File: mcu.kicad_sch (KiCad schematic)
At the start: 14 parts, among them J2 DevKit J1, J3 DevKit J3, J4 I2C / Qwiic, J5 WS2812, J6 Rail break-out, U2 74AHCT1G125

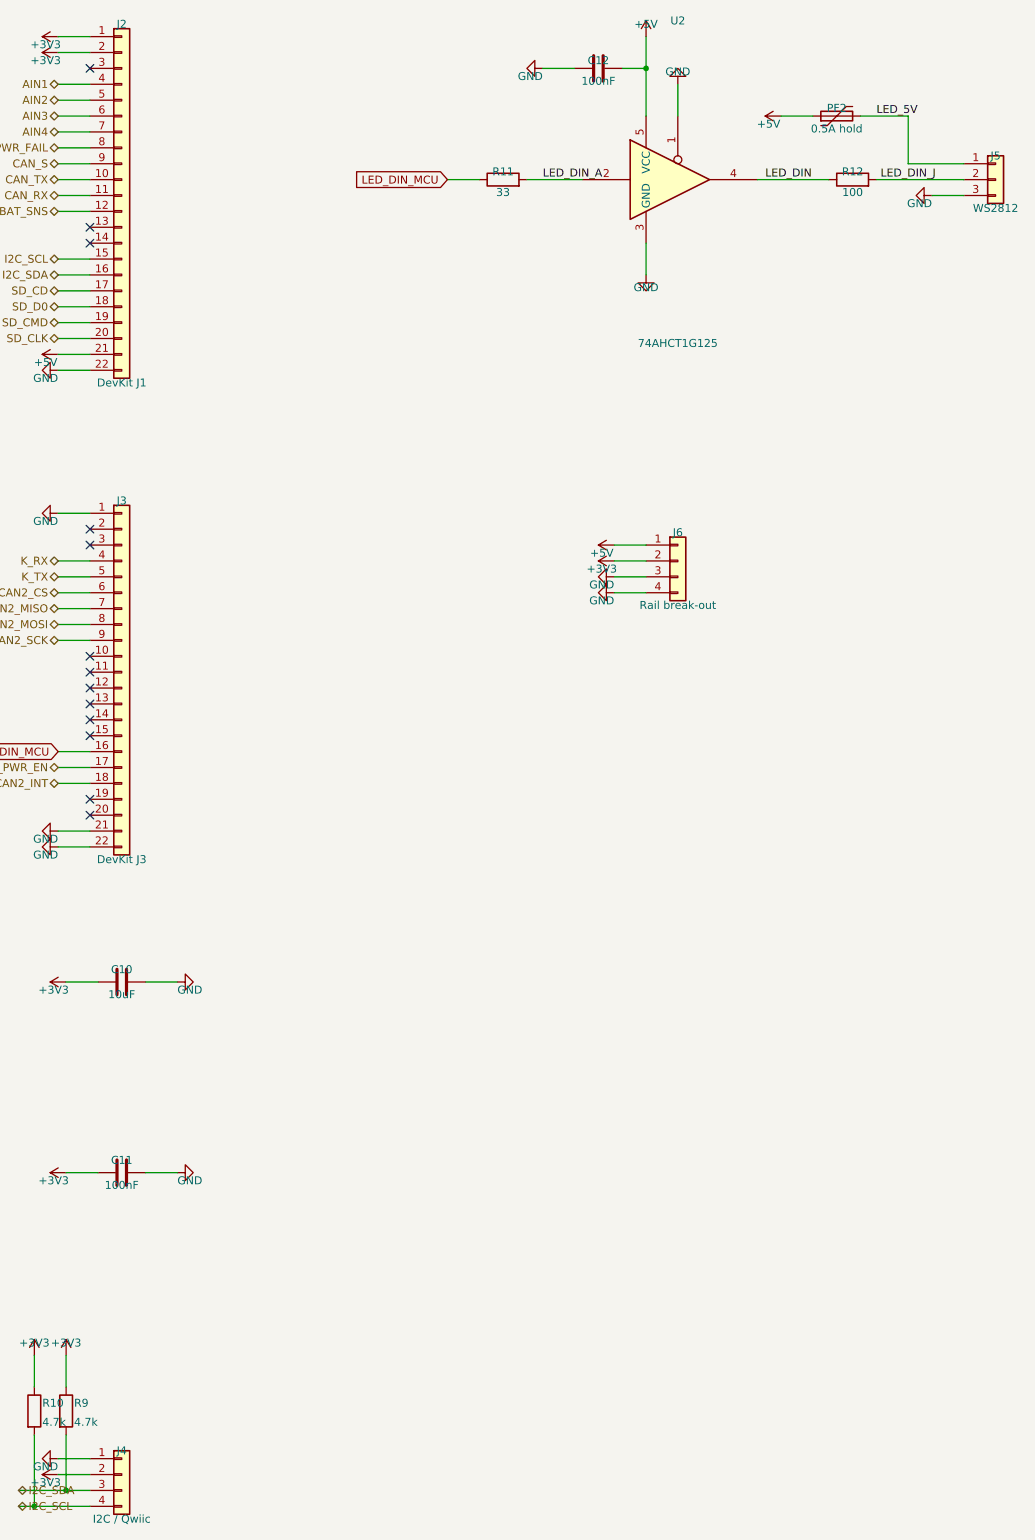
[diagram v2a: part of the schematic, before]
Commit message: Route, audit and document the carrier; verify every part number against the catalogue
Ordering is the point of this pass, so the part numbers came first. Every
LCSC number on the board was opened and read -- manufacturer part, package,
and the parameter that decides whether it is the right part. That found:

  C2148396 for the MCP2518FD    is an 18.7k resistor, out of stock -> C626759
  C255909  for a 40 MHz crystal is a 16 MHz crystal              -> C5186937
  C157966  for a JST PH 10-way  is a JST XH 9-way, 2.5 mm pitch  -> C158038

Three of the five numbers introduced last sitting were wrong, and all three
were plausible enough that the BOM exported clean. docs/PARTS.md records the
lot, including that LCSC's own listing for the microSD socket claims it has
no card-detect switch -- it has one, and the schematic is right.

Two footprints would not have soldered: both polyfuses are 1812 parts sitting
on a 1206 land, inherited from the parent board where nothing had ever
compared a part's package against its footprint. And the generic-passive
table was keyed on value alone, so the 1206 positions added last sitting
would have ordered 0805 parts -- right resistance, wrong footprint, every
board. It is keyed on (value, package) now and returns nothing rather than
guessing, so an unmatched line has no part number and somebody has to look.

Several values moved to match what is actually stocked: the power-fail
divider to 43k/18k (same trip point to 2 mV, both stocked 1 % parts), the
K-line series and pull-up to 20 R and 750 R, and the supercap charge resistor
from 22 R to 100 R -- 22 R put 1 W into a 250 mW part for the first several
seconds of every power-up.

Two real defects, both found by tools rather than by reading:

  - The hold-up Schottky was BACKWARDS. Reversed it shorts out the inrush
    limiter and blocks the discharge, so the supercap bank could never hold
    the rail up and the whole hold-up circuit was inert. audit_polarity found
    it once its expectat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
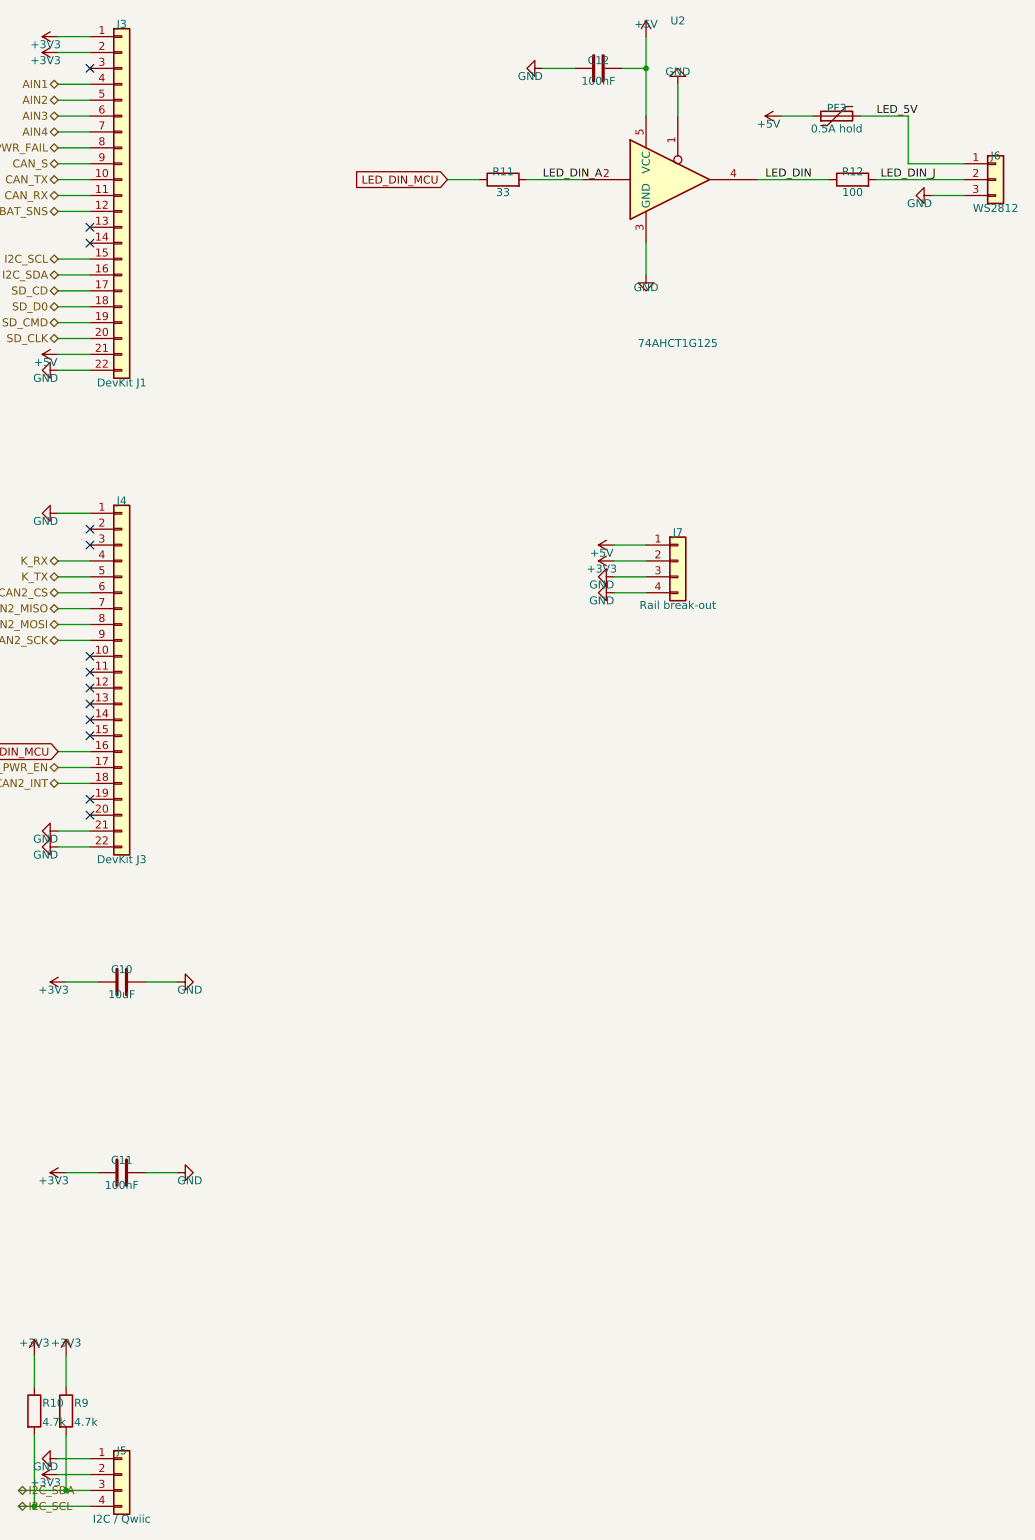
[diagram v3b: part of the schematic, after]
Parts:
- removed J2: DevKit J1, Connector_PinSocket_2.54mm:PinSocket_1x22_P2.54mm_Vertical, symbol Connector_Generic:Conn_01x22
- removed PF2: 0.5A hold, Resistor_SMD:R_1206_3216Metric, symbol Device:Polyfuse
- added J7: Rail break-out, Connector_PinHeader_2.54mm:PinHeader_1x04_P2.54mm_Vertical, symbol Connector_Generic:Conn_01x04
- added PF3: 0.5A hold, Resistor_SMD:R_1812_4532Metric, symbol Device:Polyfuse
- J3: value DevKit J3 -> DevKit J1; MPN ESP32-S3-DevKitC-1 J3 -> ESP32-S3-DevKitC-1 J1; Note Mirrors DevKitC-1 J3. K-line on 4/5, the second CAN's SPI o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 -> Mirrors DevKitC-1 J1. Pins 1-2 (3V3) and 21 (5V) are both I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
- J4: value I2C / Qwiic -> DevKit J3; footprint Connector_PinHeader_2.54mm:PinHeader_1x04_P2.54mm_Vertical -> Connector_PinSocket_2.54mm:PinSocket_1x22_P2.54mm_Vertical; symbol Connector_Generic:Conn_01x04 -> Connector_Generic:Conn_01x22; MPN (none) -> ESP32-S3-DevKitC-1 J3; Note External I2C sensors. Kept because the dev board has no Qwi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 -> Mirrors DevKitC-1 J3. K-line on 4/5, the second CAN's SPI o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
- J5: value WS2812 -> I2C / Qwiic; footprint Connector_PinHeader_2.54mm:PinHeader_1x03_P2.54mm_Vertical -> Connector_PinHeader_2.54mm:PinHeader_1x04_P2.54mm_Vertical; symbol Connector_Generic:Conn_01x03 -> Connector_Generic:Conn_01x04; Note Shift-light header: +5V / 5V-logic DIN / GND -> External I2C sensors. Kept because the dev board has no Qwi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
- J6: value Rail break-out -> WS2812; footprint Connector_PinHeader_2.54mm:PinHeader_1x04_P2.54mm_Vertical -> Connector_PinHeader_2.54mm:PinHeader_1x03_P2.54mm_Vertical; symbol Connector_Generic:Conn_01x04 -> Connector_Generic:Conn_01x03; Note (none) -> Shift-light header: +5V / 5V-logic DIN / GND
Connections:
- net +3V3: now also J3.1 (Pin_1), J3.2 (Pin_2), J5.2 (Pin_2), J7.2 (Pin_2); no longer J4.2 (Pin_2), J6.2 (Pin_2)
- net +5V: now also J3.21 (Pin_21), J7.1 (Pin_1), PF3.1; no longer J6.1 (Pin_1)
- net AIN1: now also J3.4 (Pin_4)
- net AIN2: now also J3.5 (Pin_5)
- net AIN3: now also J3.6 (Pin_6)
- net AIN4: now also J3.7 (Pin_7)
- net CAN2_CS: now also J4.6 (Pin_6); no longer J3.6 (Pin_6)
- net CAN2_INT: now also J4.18 (Pin_18); no longer J3.18 (Pin_18)
- net CAN2_MISO: now also J4.7 (Pin_7); no longer J3.7 (Pin_7)
- net CAN2_MOSI: now also J4.8 (Pin_8); no longer J3.8 (Pin_8)
- net CAN2_SCK: now also J4.9 (Pin_9); no longer J3.9 (Pin_9)
- net CAN_RX: now also J3.11 (Pin_11)
- net CAN_S: now also J3.9 (Pin_9)
- net CAN_TX: now also J3.10 (Pin_10)
- net GND: now also J4.21 (Pin_21), J4.22 (Pin_22), J5.1 (Pin_1), J7.3 (Pin_3), J7.4 (Pin_4); no longer J3.1 (Pin_1), J3.21 (Pin_21), J5.3 (Pin_3), J6.4 (Pin_4)
- net I2C_SCL: now also J3.15 (Pin_15), J5.4 (Pin_4); no longer J4.4 (Pin_4)
- net I2C_SDA: now also J3.16 (Pin_16), J5.3 (Pin_3); no longer J4.3 (Pin_3)
- net K_RX: now also J4.4 (Pin_4); no longer J3.4 (Pin_4)
- net K_TX: now also J4.5 (Pin_5); no longer J3.5 (Pin_5)
- net LED_5V: now also J6.1 (Pin_1), PF3.2; no longer J5.1 (Pin_1)
- net LED_DIN_J: now also J6.2 (Pin_2); no longer J5.2 (Pin_2)
- net LED_DIN_MCU: now also J4.16 (Pin_16); no longer J3.16 (Pin_16)
- net PWR_FAIL: now also J3.8 (Pin_8)
- net SD_CD: now also J3.17 (Pin_17)
- net SD_CLK: now also J3.20 (Pin_20)
- net SD_CMD: now also J3.19 (Pin_19)
- net SD_D0: now also J3.18 (Pin_18)
- net SD_PWR_EN: now also J4.17 (Pin_17); no longer J3.17 (Pin_17)
- net VBAT_SNS: now also J3.12 (Pin_12)
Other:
- moved on the sheet: J3
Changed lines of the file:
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@@
   (symbol (lib_id "Connector_Generic:Conn_01x22") (at 43.18 43.18 0) (unit 1)
     (in_bom yes) (on_board yes) (dnp no)
-    (property "Reference" "J2" (at 43.18 15.78 0)
+    (property "Reference" "J3" (at 43.18 15.78 0)
       (effects (font (size 1.27 1.27)) )
     )
@@
     (instances
       (project "esp32s3-can-sd-logger"
-        (path "/3276c6e6-7085-5954-8442-c6cef7eab316/a84bed91-088f-5303-a3fb-bbd35a494bf0" (reference "J2") (unit 1))
+        (path "/3276c6e6-7085-5954-8442-c6cef7eab316/a84bed91-088f-5303-a3fb-bbd35a494bf0" (reference "J3") (unit 1))
       )
     )
@@
   (symbol (lib_id "Connector_Generic:Conn_01x22") (at 43.18 119.38 0) (unit 1)
     (in_bom yes) (on_board yes) (dnp no)
-    (property "Reference" "J3" (at 43.18 91.98 0)
+    (property "Reference" "J4" (at 43.18 91.98 0)
       (effects (font (size 1.27 1.27)) )
     )
@@
     (instances
       (project "esp32s3-can-sd-logger"
-        (path "/3276c6e6-7085-5954-8442-c6cef7eab316/a84bed91-088f-5303-a3fb-bbd35a494bf0" (reference "J3") (unit 1))
+        (path "/3276c6e6-7085-5954-8442-c6cef7eab316/a84bed91-088f-5303-a3fb-bbd35a494bf0" (reference "J4") (unit 1))
       )
     )
@@
   (symbol (lib_id "Connector_Generic:Conn_01x04") (at 43.18 247.65 0) (unit 1)
     (in_bom yes) (on_board yes) (dnp no)
-    (property "Reference" "J4" (at 43.18 243.84 0)
+    (property "Reference" "J5" (at 43.18 243.84 0)
       (effects (font (size 1.27 1.27)) )
     )
@@
     (instances
       (project "esp32s3-can-sd-logger"
-        (path "/3276c6e6-7085-5954-8442-c6cef7eab316/a84bed91-088f-5303-a3fb-bbd35a494bf0" (reference "J4") (unit 1))
+        (path "/3276c6e6-7085-5954-8442-c6cef7eab316/a84bed91-088f-5303-a3fb-bbd35a494bf0" (reference "J5") (unit 1))
       )
     )
@@
   (symbol (lib_id "Device:Polyfuse") (at 157.48 30.48 90) (unit 1)
     (in_bom yes) (on_board yes) (dnp no)
-    (property "Reference" "PF2" (at 157.48 29.21 270)
+    (property "Reference" "PF3" (at 157.48 29.21 270)
       (effects (font (size 1.27 1.27)) )
     )
@@
       (effects (font (size 1.27 1.27)) )
     )
-    (property "Footprint" "Resistor_SMD:R_1206_3216Metric" (at 157.48 32.51 270)
+    (property "Footprint" "Resistor_SMD:R_1812_4532Metric" (at 157.48 32.51 270)
       (effects (font (size 1.27 1.27)) hide)
     )
@@
       (effects (font (size 1.27 1.27)) hide)
     )
-    (property "MPN" "Bourns MF-MSMF050" (at 157.48 32.51 270)
-      (effects (font (size 1.27 1.27)) hide)
-    )
-    (property "Note" "Fused tap for the shift-light strip (8x WS2812 ~0.5 A worst case)" (at 157.48 32.51 270)
-      (effects (font (size 1.27 1.27)) hide)
-    )
-    (pin "1")
-    (pin "2")
-    (instances
-      (project "esp32s3-can-sd-logger"
-        (path "/3276c6e6-7085-5954-8442-c6cef7eab316/a84bed91-088f-5303-a3fb-bbd35a494bf0" (reference "PF2") (unit 1))
+    (property "MPN" "Bourns MF-MSMF050-2" (at 157.48 32.51 270)
+      (effects (font (size 1.27 1.27)) hide)
+    )
+    (property "Note" "Fused tap for the shift-light strip (8x WS2812 ~0.5 A worst case). 1812, same correction as PF2 -- see the note there" (at 157.48 32.51 270)
+      (effects (font (size 1.27 1.27)) hide)
+    )
+    (pin "1")
+    (pin "2")
+    (instances
+      (project "esp32s3-can-sd-logger"
+        (path "/3276c6e6-7085-5954-8442-c6cef7eab316/a84bed91-088f-5303-a3fb-bbd35a494bf0" (reference "PF3") (unit 1))
       )
     )
@@
   (symbol (lib_id "Connector_Generic:Conn_01x03") (at 182.88 40.64 0) (unit 1)
     (in_bom yes) (on_board yes) (dnp no)
-    (property "Reference" "J5" (at 182.88 36.83 0)
+    (property "Reference" "J6" (at 182.88 36.83 0)
       (effects (font (size 1.27 1.27)) )
     )
@@
     (instances
       (project "esp32s3-can-sd-logger"
-        (path "/3276c6e6-7085-5954-8442-c6cef7eab316/a84bed91-088f-5303-a3fb-bbd35a494bf0" (reference "J5") (unit 1))
+        (path "/3276c6e6-7085-5954-8442-c6cef7eab316/a84bed91-088f-5303-a3fb-bbd35a494bf0" (reference "J6") (unit 1))
       )
     )
@@
   (symbol (lib_id "Connector_Generic:Conn_01x04") (at 132.08 101.6 0) (unit 1)
     (in_bom yes) (on_board yes) (dnp no)
-    (property "Reference" "J6" (at 132.08 97.06 0)
+    (property "Reference" "J7" (at 132.08 97.06 0)
       (effects (font (size 1.27 1.27)) )
     )
@@
     (instances
       (project "esp32s3-can-sd-logger"
-        (path "/3276c6e6-7085-5954-8442-c6cef7eab316/a84bed91-088f-5303-a3fb-bbd35a494bf0" (reference "J6") (unit 1))
-      )
-    )
+        (path "/3276c6e6-7085-5954-8442-c6cef7eab316/a84bed91-088f-5303-a3fb-bbd35a494bf0" (reference "J7") (unit 1))
+      )
+    )
